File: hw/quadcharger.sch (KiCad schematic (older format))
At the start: 3 parts, among them J2 Conn_01x08, U2 MCP23017_SS, U5 4052

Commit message: multiple changes
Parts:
- added C25: 100n, Capacitor_SMD:C_0805_2012Metric_Pad1.15x1.40mm_HandSolder, symbol Device:C_Small
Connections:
- net +5V: now also C25.1; no longer U5.16 (VDD)
- net GND: now also C25.2
- new net +5VA: U5.16 (VDD)
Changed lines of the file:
@@
 $Descr A4 11693 8268
 encoding utf-8
-Sheet 2 15
+Sheet 7 15
 Title ""
 Date ""
@@
 F8 "L-" O R 8000 1300 50
 $EndSheet
-$Comp
-L Interface_Expansion:MCP23017_SS U2
-U 1 1 5DC5AB33
-P 3600 3150
-AR Path="/5DC581CC/5DC5AB33" Ref="U2"  Part="1"
-AR Path="/5DC82B0A/5DC5AB33" Ref="U12"  Part="1"
-AR Path="/5DE36E4E/5DC5AB33" Ref="U?"  Part="1"
-AR Path="/5DE37049/5DC5AB33" Ref="U?"  Part="1"
-F 0 "U12" H 3050 4350 50  0000 C CNN
-F 1 "MCP23017_SS" H 3250 4250 50  0000 C CNN
-F 2 "Package_SO:SSOP-28_5.3x10.2mm_P0.65mm" H 3800 2150 50  0001 L CNN
-F 3 "http://ww1.microchip.com/downloads/en/DeviceDoc/20001952C.pdf" H 3800 2050 50  0001 L CNN
-	1    3600 3150
-	1    0    0    -1
-$EndComp
 $Sheet
 S 7450 2200 550  800
@@
 Wire Wire Line
 	6450 5200 7450 5200
-$Comp
-L 4xxx:4052 U5
-U 1 1 5DC60E58
-P 5600 4850
-AR Path="/5DC581CC/5DC60E58" Ref="U5"  Part="1"
-AR Path="/5DC82B0A/5DC60E58" Ref="U15"  Part="1"
-AR Path="/5DE36E4E/5DC60E58" Ref="U?"  Part="1"
-AR Path="/5DE37049/5DC60E58" Ref="U?"  Part="1"
-F 0 "U15" H 5850 5800 50  0000 C CNN
-F 1 "4052" H 5850 5700 50  0000 C CNN
-F 2 "Package_SO:TSSOP-16_4.4x5mm_P0.65mm" H 5600 4850 50  0001 C CNN
-F 3 "http://www.intersil.com/content/dam/Intersil/documents/cd40/cd4051bms-52bms-53bms.pdf" H 5600 4850 50  0001 C CNN
-	1    5600 4850
-	1    0    0    -1
-$EndComp
 Text Label 7350 1200 2    50   ~ 0
 X0
@@
 Wire Wire Line
 	7350 4750 7450 4750
-Wire Wire Line
-	4900 5350 5100 5350
 Text Label 5100 4250 2    50   ~ 0
 X0
@@
 Wire Wire Line
 	4300 3750 4800 3750
-Wire Wire Line
-	4800 5450 5100 5450
 $Comp
 L power:GND #PWR0108
@@
 Text HLabel 2900 2450 0    50   Input ~ 0
 SCK
-$Comp
-L power:+5V #PWR0110
-U 1 1 5DC74DCC
-P 3600 2050
-AR Path="/5DC581CC/5DC74DCC" Ref="#PWR0110"  Part="1"
-AR Path="/5DC82B0A/5DC74DCC" Ref="#PWR0152"  Part="1"
-AR Path="/5DE36E4E/5DC74DCC" Ref="#PWR?"  Part="1"
-AR Path="/5DE37049/5DC74DCC" Ref="#PWR?"  Part="1"
-F 0 "#PWR0152" H 3600 1900 50  0001 C CNN
-F 1 "+5V" H 3600 2200 50  0000 C CNN
-F 2 "" H 3600 2050 50  0001 C CNN
-F 3 "" H 3600 2050 50  0001 C CNN
-	1    3600 2050
-	1    0    0    -1
-$EndComp
 Wire Wire Line
 	9350 3100 8250 3100
@@
 Text HLabel 6100 4650 2    50   Output ~ 0
 VD
-$Comp
-L power:+5V #PWR0114
-U 1 1 5DCAA6F6
-P 5600 3950
-AR Path="/5DC581CC/5DCAA6F6" Ref="#PWR0114"  Part="1"
-AR Path="/5DC82B0A/5DCAA6F6" Ref="#PWR0156"  Part="1"
-AR Path="/5DE36E4E/5DCAA6F6" Ref="#PWR?"  Part="1"
-AR Path="/5DE37049/5DCAA6F6" Ref="#PWR?"  Part="1"
-F 0 "#PWR0156" H 5600 3800 50  0001 C CNN
-F 1 "+5V" H 5600 4100 50  0000 C CNN
-F 2 "" H 5600 3950 50  0001 C CNN
-F 3 "" H 5600 3950 50  0001 C CNN
-	1    5600 3950
-	1    0    0    -1
-$EndComp
 Wire Wire Line
 	4450 3950 4300 3950
@@
 $EndComp
 NoConn ~ 4450 3950
+Wire Wire Line
+	3600 2050 3600 1900
+$Comp
+L power:GND #PWR0103
+U 1 1 5DCA0037
+P 3850 2100
+AR Path="/5DC581CC/5DCA0037" Ref="#PWR0103"  Part="1"
+AR Path="/5DC82B0A/5DCA0037" Ref="#PWR0114"  Part="1"
+F 0 "#PWR0114" H 3850 1850 50  0001 C CNN
+F 1 "GND" H 4000 2050 50  0000 C CNN
+F 2 "" H 3850 2100 50  0001 C CNN
+F 3 "" H 3850 2100 50  0001 C CNN
+	1    3850 2100
+	1    0    0    -1
+$EndComp
+Wire Wire Line
+	3700 1900 3850 1900
+Connection ~ 3700 1900
+Wire Wire Line
+	3700 1800 3700 1900
+Wire Wire Line
+	3600 1900 3700 1900
+$Comp
+L Device:C_Small C25
+U 1 1 5DC9B25F
+P 3850 2000
+AR Path="/5DC581CC/5DC9B25F" Ref="C25"  Part="1"
+AR Path="/5DC82B0A/5DC9B25F" Ref="C27"  Part="1"
+F 0 "C27" H 3942 2046 50  0000 L CNN
+F 1 "100n" H 3942 1955 50  0000 L CNN
+F 2 "Capacitor_SMD:C_0805_2012Metric_Pad1.15x1.40mm_HandSolder" H 3850 2000 50  0001 C CNN
+F 3 "~" H 3850 2000 50  0001 C CNN
+	1    3850 2000
+	1    0    0    -1
+$EndComp
+$Comp
+L power:+5V #PWR0110
+U 1 1 5DC74DCC
+P 3700 1800
+AR Path="/5DC581CC/5DC74DCC" Ref="#PWR0110"  Part="1"
+AR Path="/5DC82B0A/5DC74DCC" Ref="#PWR0152"  Part="1"
+AR Path="/5DE36E4E/5DC74DCC" Ref="#PWR?"  Part="1"
+AR Path="/5DE37049/5DC74DCC" Ref="#PWR?"  Part="1"
+F 0 "#PWR0152" H 3700 1650 50  0001 C CNN
+F 1 "+5V" H 3700 1950 50  0000 C CNN
+F 2 "" H 3700 1800 50  0001 C CNN
+F 3 "" H 3700 1800 50  0001 C CNN
+	1    3700 1800
+	1    0    0    -1
+$EndComp
+$Comp
+L Interface_Expansion:MCP23017_SS U2
+U 1 1 5DC5AB33
+P 3600 3150
+AR Path="/5DC581CC/5DC5AB33" Ref="U2"  Part="1"
+AR Path="/5DC82B0A/5DC5AB33" Ref="U12"  Part="1"
+AR Path="/5DE36E4E/5DC5AB33" Ref="U?"  Part="1"
+AR Path="/5DE37049/5DC5AB33" Ref="U?"  Part="1"
+F 0 "U12" H 3050 4350 50  0000 C CNN
+F 1 "MCP23017_SS" H 3250 4250 50  0000 C CNN
+F 2 "Package_SO:SSOP-28_5.3x10.2mm_P0.65mm" H 3800 2150 50  0001 L CNN
+F 3 "http://ww1.microchip.com/downloads/en/DeviceDoc/20001952C.pdf" H 3800 2050 50  0001 L CNN
+	1    3600 3150
+	1    0    0    -1
+$EndComp
+Wire Wire Line
+	4800 5450 5100 5450
+Wire Wire Line
+	4900 5350 5100 5350
+$Comp
+L 4xxx:4052 U5
+U 1 1 5DC60E58
+P 5600 4850
+AR Path="/5DC581CC/5DC60E58" Ref="U5"  Part="1"
+AR Path="/5DC82B0A/5DC60E58" Ref="U15"  Part="1"
+AR Path="/5DE36E4E/5DC60E58" Ref="U?"  Part="1"
+AR Path="/5DE37049/5DC60E58" Ref="U?"  Part="1"
+F 0 "U15" H 5450 5750 50  0000 C CNN
+F 1 "4052" H 5400 5650 50  0000 C CNN
+F 2 "Package_SO:TSSOP-16_4.4x5mm_P0.65mm" H 5600 4850 50  0001 C CNN
+F 3 "http://www.intersil.com/content/dam/Intersil/documents/cd40/cd4051bms-52bms-53bms.pdf" H 5600 4850 50  0001 C CNN
+	1    5600 4850
+	1    0    0    -1
+$EndComp
+$Comp
+L power:+5VA #PWR0101
+U 1 1 5DC92534
+P 5600 3950
+AR Path="/5DC581CC/5DC92534" Ref="#PWR0101"  Part="1"
+AR Path="/5DC82B0A/5DC92534" Ref="#PWR0102"  Part="1"
+F 0 "#PWR0102" H 5600 3800 50  0001 C CNN
+F 1 "+5VA" H 5615 4123 50  0000 C CNN
+F 2 "" H 5600 3950 50  0001 C CNN
+F 3 "" H 5600 3950 50  0001 C CNN
+	1    5600 3950
+	1    0    0    -1
+$EndComp
 $EndSCHEMATC

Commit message: hw: pcb redesign
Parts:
- removed J2: Conn_01x08, Connector_JST:JST_XH_B8B-XH-A_1x08_P2.50mm_Vertical, symbol Connector_Generic:Conn_01x08
- U2: footprint Package_SO:SSOP-28_5.3x10.2mm_P0.65mm -> Package_SO:SOIC-28W_7.5x17.9mm_P1.27mm
- U5: value 4052 -> 74HC4052; footprint Package_SO:TSSOP-16_4.4x5mm_P0.65mm -> Package_SO:SO-16_5.3x10.2mm_P1.27mm
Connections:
- net GND: now also U2.10 (VSS), U5.6 (Inh)
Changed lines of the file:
@@
 EESchema Schematic File Version 4
-LIBS:charger2-cache
 EELAYER 30 0
 EELAYER END
 $Descr A4 11693 8268
 encoding utf-8
-Sheet 7 15
+Sheet 7 17
 Title ""
 Date ""
@@
 Comment4 ""
 $EndDescr
-$Sheet
-S 7450 1050 550  800
-U 5DC581FA
-F0 "Battery" 50
-F1 "Battery.sch" 50
-F2 "CE" I L 7450 1500 50
-F3 "CHRG" O L 7450 1750 50
-F4 "DE" I L 7450 1600 50
-F5 "VB" O L 7450 1200 50
-F6 "VD" O L 7450 1300 50
-F7 "L+" O R 8000 1200 50
-F8 "L-" O R 8000 1300 50
-$EndSheet
-$Sheet
-S 7450 2200 550  800
-U 5DC5D939
-F0 "sheet5DC5D930" 50
-F1 "Battery.sch" 50
-F2 "CE" I L 7450 2650 50
-F3 "CHRG" O L 7450 2900 50
-F4 "DE" I L 7450 2750 50
-F5 "VB" O L 7450 2350 50
-F6 "VD" O L 7450 2450 50
-F7 "L+" O R 8000 2350 50
-F8 "L-" O R 8000 2450 50
-$EndSheet
-$Sheet
-S 7450 3350 550  800
-U 5DC5D9F3
-F0 "sheet5DC5D9EA" 50
-F1 "Battery.sch" 50
-F2 "CE" I L 7450 3800 50
-F3 "CHRG" O L 7450 4050 50
-F4 "DE" I L 7450 3900 50
-F5 "VB" O L 7450 3500 50
-F6 "VD" O L 7450 3600 50
-F7 "L+" O R 8000 3500 50
-F8 "L-" O R 8000 3600 50
-$EndSheet
-$Sheet
-S 7450 4500 550  800
-U 5DC5DB65
-F0 "sheet5DC5DB5C" 50
-F1 "Battery.sch" 50
-F2 "CE" I L 7450 4950 50
-F3 "CHRG" O L 7450 5200 50
-F4 "DE" I L 7450 5050 50
-F5 "VB" O L 7450 4650 50
-F6 "VD" O L 7450 4750 50
-F7 "L+" O R 8000 4650 50
-F8 "L-" O R 8000 4750 50
-$EndSheet
 Wire Wire Line
 	4300 2350 6600 2350
@@
 Text HLabel 2900 2450 0    50   Input ~ 0
 SCK
-Wire Wire Line
-	9350 3100 8250 3100
-Wire Wire Line
-	8250 3100 8250 2450
-Wire Wire Line
-	8250 2450 8000 2450
-Wire Wire Line
-	8000 3500 8250 3500
-Wire Wire Line
-	8250 3500 8250 3200
-Wire Wire Line
-	8250 3200 9350 3200
-Wire Wire Line
-	9350 3300 8350 3300
-Wire Wire Line
-	8350 3300 8350 3600
-Wire Wire Line
-	8350 3600 8000 3600
-Wire Wire Line
-	8000 2350 8350 2350
-Wire Wire Line
-	8350 2350 8350 3000
-Wire Wire Line
-	8350 3000 9350 3000
-Wire Wire Line
-	9350 3400 8450 3400
-Wire Wire Line
-	8450 3400 8450 4650
-Wire Wire Line
-	8450 4650 8000 4650
-Wire Wire Line
-	8000 4750 8600 4750
-Wire Wire Line
-	8600 4750 8600 3500
-Wire Wire Line
-	8600 3500 9350 3500
-Wire Wire Line
-	9350 2900 8450 2900
-Wire Wire Line
-	8450 2900 8450 1300
-Wire Wire Line
-	8450 1300 8000 1300
-Wire Wire Line
-	8000 1200 8550 1200
-Wire Wire Line
-	8550 1200 8550 2800
-Wire Wire Line
-	8550 2800 9350 2800
 Text HLabel 6100 4250 2    50   Output ~ 0
 VB
@@
 	6950 3250 4300 3250
 NoConn ~ 4300 3850
-$Comp
-L Connector_Generic:Conn_01x08 J2
-U 1 1 5DC76FC9
-P 9550 3100
-AR Path="/5DC581CC/5DC76FC9" Ref="J2"  Part="1"
-AR Path="/5DC82B0A/5DC76FC9" Ref="J3"  Part="1"
-AR Path="/5DE36E4E/5DC76FC9" Ref="J?"  Part="1"
-AR Path="/5DE37049/5DC76FC9" Ref="J?"  Part="1"
-F 0 "J3" H 9630 3092 50  0000 L CNN
-F 1 "Conn_01x08" H 9630 3001 50  0000 L CNN
-F 2 "Connector_JST:JST_XH_B8B-XH-A_1x08_P2.50mm_Vertical" H 9550 3100 50  0001 C CNN
-F 3 "~" H 9550 3100 50  0001 C CNN
-	1    9550 3100
-	1    0    0    -1
-$EndComp
 NoConn ~ 4450 3950
 Wire Wire Line
@@
 F 0 "U12" H 3050 4350 50  0000 C CNN
 F 1 "MCP23017_SS" H 3250 4250 50  0000 C CNN
-F 2 "Package_SO:SSOP-28_5.3x10.2mm_P0.65mm" H 3800 2150 50  0001 L CNN
+F 2 "Package_SO:SOIC-28W_7.5x17.9mm_P1.27mm" H 3800 2150 50  0001 L CNN
 F 3 "http://ww1.microchip.com/downloads/en/DeviceDoc/20001952C.pdf" H 3800 2050 50  0001 L CNN
 	1    3600 3150
@@
 AR Path="/5DE37049/5DC60E58" Ref="U?"  Part="1"
 F 0 "U15" H 5450 5750 50  0000 C CNN
-F 1 "4052" H 5400 5650 50  0000 C CNN
-F 2 "Package_SO:TSSOP-16_4.4x5mm_P0.65mm" H 5600 4850 50  0001 C CNN
+F 1 "74HC4052" H 5400 5650 50  0000 C CNN
+F 2 "Package_SO:SO-16_5.3x10.2mm_P1.27mm" H 5600 4850 50  0001 C CNN
 F 3 "http://www.intersil.com/content/dam/Intersil/documents/cd40/cd4051bms-52bms-53bms.pdf" H 5600 4850 50  0001 C CNN
 	1    5600 4850
@@
 	1    0    0    -1
 $EndComp
+$Comp
+L power:GND #PWR0111
+U 1 1 5F95C640
+P 3600 4250
+AR Path="/5DC581CC/5F95C640" Ref="#PWR0111"  Part="1"
+AR Path="/5DC82B0A/5F95C640" Ref="#PWR0161"  Part="1"
+F 0 "#PWR0161" H 3600 4000 50  0001 C CNN
+F 1 "GND" H 3605 4077 50  0000 C CNN
+F 2 "" H 3600 4250 50  0001 C CNN
+F 3 "" H 3600 4250 50  0001 C CNN
+	1    3600 4250
+	1    0    0    -1
+$EndComp
+$Comp
+L power:GND #PWR0112
+U 1 1 5F95EFD1
+P 5050 5200
+AR Path="/5DC581CC/5F95EFD1" Ref="#PWR0112"  Part="1"
+AR Path="/5DC82B0A/5F95EFD1" Ref="#PWR0162"  Part="1"
+F 0 "#PWR0162" H 5050 4950 50  0001 C CNN
+F 1 "GND" H 5055 5027 50  0000 C CNN
+F 2 "" H 5050 5200 50  0001 C CNN
+F 3 "" H 5050 5200 50  0001 C CNN
+	1    5050 5200
+	1    0    0    -1
+$EndComp
+Wire Wire Line
+	5050 5200 5050 5150
+Wire Wire Line
+	5050 5150 5100 5150
+$Sheet
+S 7450 4500 550  800
+U 5DC5DB65
+F0 "sheet5DC5DB5C" 50
+F1 "Battery.sch" 50
+F2 "CE" I L 7450 4950 50
+F3 "CHRG" O L 7450 5200 50
+F4 "DE" I L 7450 5050 50
+F5 "VB" O L 7450 4650 50
+F6 "VD" O L 7450 4750 50
+F7 "TEMP" O R 8000 4900 50
+$EndSheet
+$Sheet
+S 7450 3350 550  800
+U 5DC5D9F3
+F0 "sheet5DC5D9EA" 50
+F1 "Battery.sch" 50
+F2 "CE" I L 7450 3800 50
+F3 "CHRG" O L 7450 4050 50
+F4 "DE" I L 7450 3900 50
+F5 "VB" O L 7450 3500 50
+F6 "VD" O L 7450 3600 50
+F7 "TEMP" O R 8000 3750 50
+$EndSheet
+$Sheet
+S 7450 1050 550  800
+U 5DC581FA
+F0 "Battery" 50
+F1 "Battery.sch" 50
+F2 "CE" I L 7450 1500 50
+F3 "CHRG" O L 7450 1750 50
+F4 "DE" I L 7450 1600 50
+F5 "VB" O L 7450 1200 50
+F6 "VD" O L 7450 1300 50
+F7 "TEMP" O R 8000 1400 50
+$EndSheet
+$Sheet
+S 7450 2200 550  800
+U 5DC5D939
+F0 "sheet5DC5D930" 50
+F1 "Battery.sch" 50
+F2 "CE" I L 7450 2650 50
+F3 "CHRG" O L 7450 2900 50
+F4 "DE" I L 7450 2750 50
+F5 "VB" O L 7450 2350 50
+F6 "VD" O L 7450 2450 50
+F7 "TEMP" O R 8000 2550 50
+$EndSheet
+Text HLabel 8400 1400 2    50   Output ~ 0
+T1
+Wire Wire Line
+	8400 1400 8000 1400
+Text HLabel 8400 2550 2    50   Output ~ 0
+T2
+Wire Wire Line
+	8400 2550 8000 2550
+Text HLabel 8400 3750 2    50   Output ~ 0
+T3
+Wire Wire Line
+	8400 3750 8000 3750
+Text HLabel 8400 4900 2    50   Output ~ 0
+T4
+Wire Wire Line
+	8400 4900 8000 4900
 $EndSCHEMATC

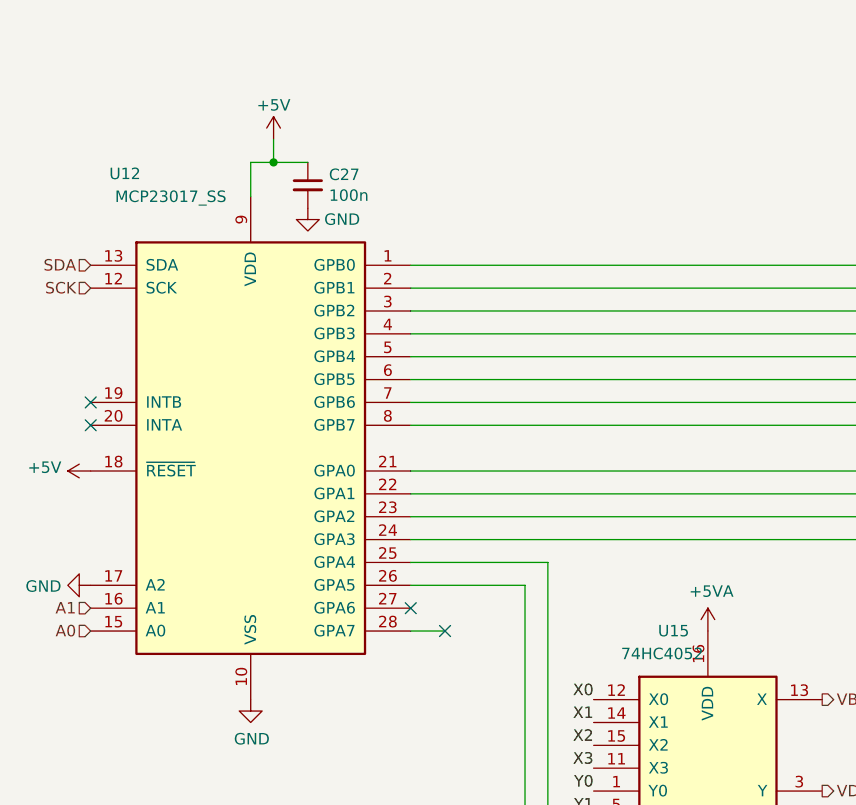
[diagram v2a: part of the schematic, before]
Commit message: fix 4052 footprint
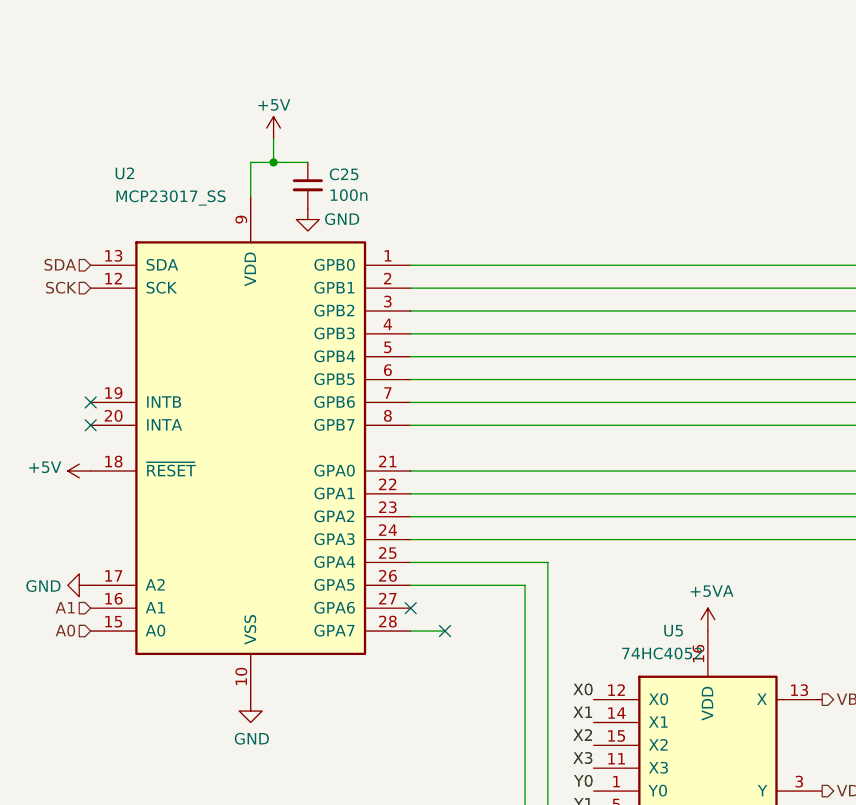
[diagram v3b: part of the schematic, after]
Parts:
- U5: footprint Package_SO:SO-16_5.3x10.2mm_P1.27mm -> Package_SO:SO-16_3.9x9.9mm_P1.27mm
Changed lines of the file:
@@
 $Descr A4 11693 8268
 encoding utf-8
-Sheet 7 17
+Sheet 2 17
 Title ""
 Date ""
@@
 AR Path="/5DE36E4E/5DC72102" Ref="#PWR?"  Part="1"
 AR Path="/5DE37049/5DC72102" Ref="#PWR?"  Part="1"
-F 0 "#PWR0150" H 2900 3500 50  0001 C CNN
+F 0 "#PWR0108" H 2900 3500 50  0001 C CNN
 F 1 "GND" V 2905 3622 50  0000 R CNN
 F 2 "" H 2900 3750 50  0001 C CNN
@@
 AR Path="/5DE36E4E/5DC72E27" Ref="#PWR?"  Part="1"
 AR Path="/5DE37049/5DC72E27" Ref="#PWR?"  Part="1"
-F 0 "#PWR0151" H 2900 3100 50  0001 C CNN
+F 0 "#PWR0109" H 2900 3100 50  0001 C CNN
 F 1 "+5V" V 2915 3378 50  0000 L CNN
 F 2 "" H 2900 3250 50  0001 C CNN
@@
 AR Path="/5DC82B0A/5E10AAB0" Ref="#PWR0222"  Part="1"
 AR Path="/5DC581CC/5E10AAB0" Ref="#PWR0221"  Part="1"
-F 0 "#PWR0222" H 5650 5600 50  0001 C CNN
+F 0 "#PWR0221" H 5650 5600 50  0001 C CNN
 F 1 "GND" H 5655 5677 50  0000 C CNN
 F 2 "" H 5650 5850 50  0001 C CNN
@@
 AR Path="/5DC581CC/5DCA0037" Ref="#PWR0103"  Part="1"
 AR Path="/5DC82B0A/5DCA0037" Ref="#PWR0114"  Part="1"
-F 0 "#PWR0114" H 3850 1850 50  0001 C CNN
+F 0 "#PWR0103" H 3850 1850 50  0001 C CNN
 F 1 "GND" H 4000 2050 50  0000 C CNN
 F 2 "" H 3850 2100 50  0001 C CNN
@@
 AR Path="/5DC581CC/5DC9B25F" Ref="C25"  Part="1"
 AR Path="/5DC82B0A/5DC9B25F" Ref="C27"  Part="1"
-F 0 "C27" H 3942 2046 50  0000 L CNN
+F 0 "C25" H 3942 2046 50  0000 L CNN
 F 1 "100n" H 3942 1955 50  0000 L CNN
 F 2 "Capacitor_SMD:C_0805_2012Metric_Pad1.15x1.40mm_HandSolder" H 3850 2000 50  0001 C CNN
@@
 AR Path="/5DE36E4E/5DC74DCC" Ref="#PWR?"  Part="1"
 AR Path="/5DE37049/5DC74DCC" Ref="#PWR?"  Part="1"
-F 0 "#PWR0152" H 3700 1650 50  0001 C CNN
+F 0 "#PWR0110" H 3700 1650 50  0001 C CNN
 F 1 "+5V" H 3700 1950 50  0000 C CNN
 F 2 "" H 3700 1800 50  0001 C CNN
@@
 AR Path="/5DE36E4E/5DC5AB33" Ref="U?"  Part="1"
 AR Path="/5DE37049/5DC5AB33" Ref="U?"  Part="1"
-F 0 "U12" H 3050 4350 50  0000 C CNN
+F 0 "U2" H 3050 4350 50  0000 C CNN
 F 1 "MCP23017_SS" H 3250 4250 50  0000 C CNN
 F 2 "Package_SO:SOIC-28W_7.5x17.9mm_P1.27mm" H 3800 2150 50  0001 L CNN
@@
 AR Path="/5DE36E4E/5DC60E58" Ref="U?"  Part="1"
 AR Path="/5DE37049/5DC60E58" Ref="U?"  Part="1"
-F 0 "U15" H 5450 5750 50  0000 C CNN
+F 0 "U5" H 5450 5750 50  0000 C CNN
 F 1 "74HC4052" H 5400 5650 50  0000 C CNN
-F 2 "Package_SO:SO-16_5.3x10.2mm_P1.27mm" H 5600 4850 50  0001 C CNN
+F 2 "Package_SO:SO-16_3.9x9.9mm_P1.27mm" H 5600 4850 50  0001 C CNN
 F 3 "http://www.intersil.com/content/dam/Intersil/documents/cd40/cd4051bms-52bms-53bms.pdf" H 5600 4850 50  0001 C CNN
 	1    5600 4850
@@
 AR Path="/5DC581CC/5DC92534" Ref="#PWR0101"  Part="1"
 AR Path="/5DC82B0A/5DC92534" Ref="#PWR0102"  Part="1"
-F 0 "#PWR0102" H 5600 3800 50  0001 C CNN
+F 0 "#PWR0101" H 5600 3800 50  0001 C CNN
 F 1 "+5VA" H 5615 4123 50  0000 C CNN
 F 2 "" H 5600 3950 50  0001 C CNN
@@
 AR Path="/5DC581CC/5F95C640" Ref="#PWR0111"  Part="1"
 AR Path="/5DC82B0A/5F95C640" Ref="#PWR0161"  Part="1"
-F 0 "#PWR0161" H 3600 4000 50  0001 C CNN
+F 0 "#PWR0111" H 3600 4000 50  0001 C CNN
 F 1 "GND" H 3605 4077 50  0000 C CNN
 F 2 "" H 3600 4250 50  0001 C CNN
@@
 AR Path="/5DC581CC/5F95EFD1" Ref="#PWR0112"  Part="1"
 AR Path="/5DC82B0A/5F95EFD1" Ref="#PWR0162"  Part="1"
-F 0 "#PWR0162" H 5050 4950 50  0001 C CNN
+F 0 "#PWR0112" H 5050 4950 50  0001 C CNN
 F 1 "GND" H 5055 5027 50  0000 C CNN
 F 2 "" H 5050 5200 50  0001 C CNN
